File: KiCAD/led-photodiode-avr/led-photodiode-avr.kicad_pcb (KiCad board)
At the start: 4 copper layers, 68.6 x 80 mm, 85 parts, among them J1 Screw_Terminal_01x02, J2 Conn_02x08_Odd_Even, J3 ISP, J4 Conn_01x06_Pin, Q1 TTC1949, Q2 TTC1949, Q3 TTC1949, Q4 TTC1949, Q5 TTC1949, Q6 TTC1949, Q7 TTC1949, Q8 TTC1949, U1 REF3040AIDBZT, U10 AZ1117CH2-5.0, U11 MCP3221, U2 AZ1117CH2-5.0, U3 OPA365xxD, U5 DDC112, U6 LTC1380, U7 ATmega328-A, U8 OPA365AIDR, U9 LTC2631, Y1 CO_16MHZ

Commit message: working on v2 layout
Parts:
- removed N1: Optical_PCB, optical_pcb_model:optical_pcb
- added C27: 0.1uF, Capacitor_SMD:C_0805_2012Metric_Pad1.18x1.45mm_HandSolder, F.Cu at (150.5, 82.4)
- C19, C20, C24, C25: footprint Capacitor_SMD:C_0805_2012Metric_Pad1.18x1.45mm_HandSolder -> Capacitor_SMD:C_0603_1608Metric_Pad1.08x0.95mm_HandSolder
- moved TP4 77.0 mm to (126.5, 77.6)
- moved C24 67.0 mm to (158.5, 123.7), turned to 180 degrees
- moved TP1 65.0 mm to (137.7, 92.6)
- moved TP7 64.2 mm to (143.9, 106.8)
- moved TP3 62.2 mm to (139.8, 95.5)
- moved TP5 55.9 mm to (152.3, 97.8)
- moved TP6 54.4 mm to (152.3, 95.4)
- moved C25 53.8 mm to (162.9, 109.9)
- moved TP2 50.0 mm to (152.3, 93.1)
- moved C26 45.9 mm to (150.6, 75.8), turned to 180 degrees
- moved R12 45.8 mm to (156.6, 83.8), turned to -90 degrees
- moved U11 45.7 mm to (150.5, 79.1), turned to 180 degrees
- moved Q8 39.7 mm to (156.2, 89.5), turned to -90 degrees
- moved Q7 35.4 mm to (160.0, 89.5), turned to -90 degrees
- moved Q6 31.6 mm to (163.8, 89.5), turned to -90 degrees
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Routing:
- net /TSENSE: track 0.00 -> 34.6 mm, vias 0 -> 3
- net (no net): track 27.3 -> 0.00 mm
- net Net-(Q1-B): track 9.35 -> 30.2 mm, vias 0 -> 2
- net Net-(Q5-B): track 0.00 -> 20.7 mm, vias 0 -> 2
- net Net-(Q8-B): track 0.00 -> 19.5 mm, vias 0 -> 2
- net Net-(Q7-B): track 0.00 -> 18.9 mm, vias 0 -> 2
- net Net-(Q6-B): track 0.00 -> 18.3 mm, vias 0 -> 2
- net Net-(Q2-B): track 10.4 -> 27.6 mm, vias 0 -> 2
- net Net-(Q3-B): track 12.7 -> 26.1 mm, vias 0 -> 2
- net /LED_driver/LED_1: track 21.9 -> 8.78 mm, vias 1 -> 0
- net /PD7: track 38.5 -> 45.1 mm, vias 2 -> 3
- net /LED_driver/LED_2: track 1.27 -> 7.51 mm, vias 1 -> 0
- net /LED_driver/LED_8: track 0.00 -> 6.21 mm
- net Net-(Q4-B): track 16.7 -> 22.8 mm, vias 0 -> 2
- net /LED_driver/LED_5: track 0.00 -> 5.89 mm
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- added copper zone on F.Cu, net Net-(Q1-E)
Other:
- board text added: "NIR Wearable Optical Test V2.0 -2025-10 E. Hazen"
- board text removed: "NIR Wearable Optical Test V1.0 -2025-08 E. Hazen"

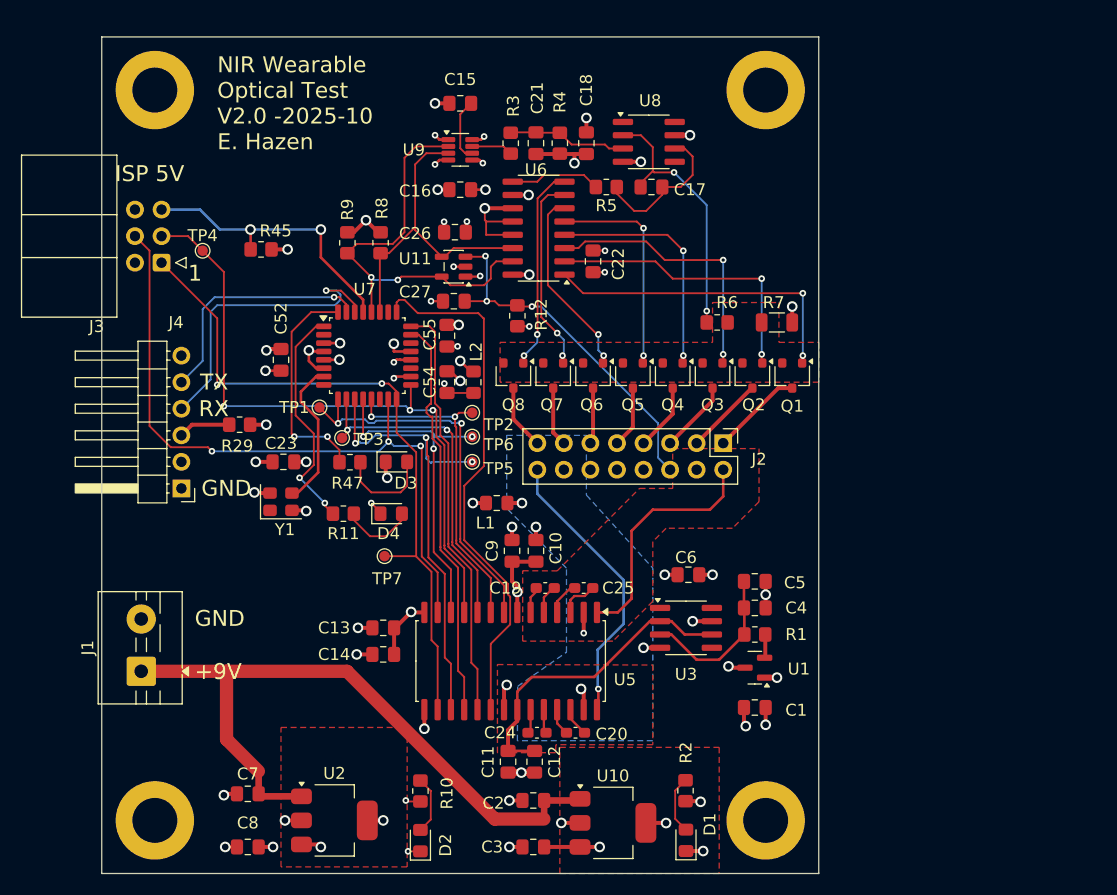
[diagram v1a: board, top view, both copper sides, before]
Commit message: Add op-amp buffer on temp sensor
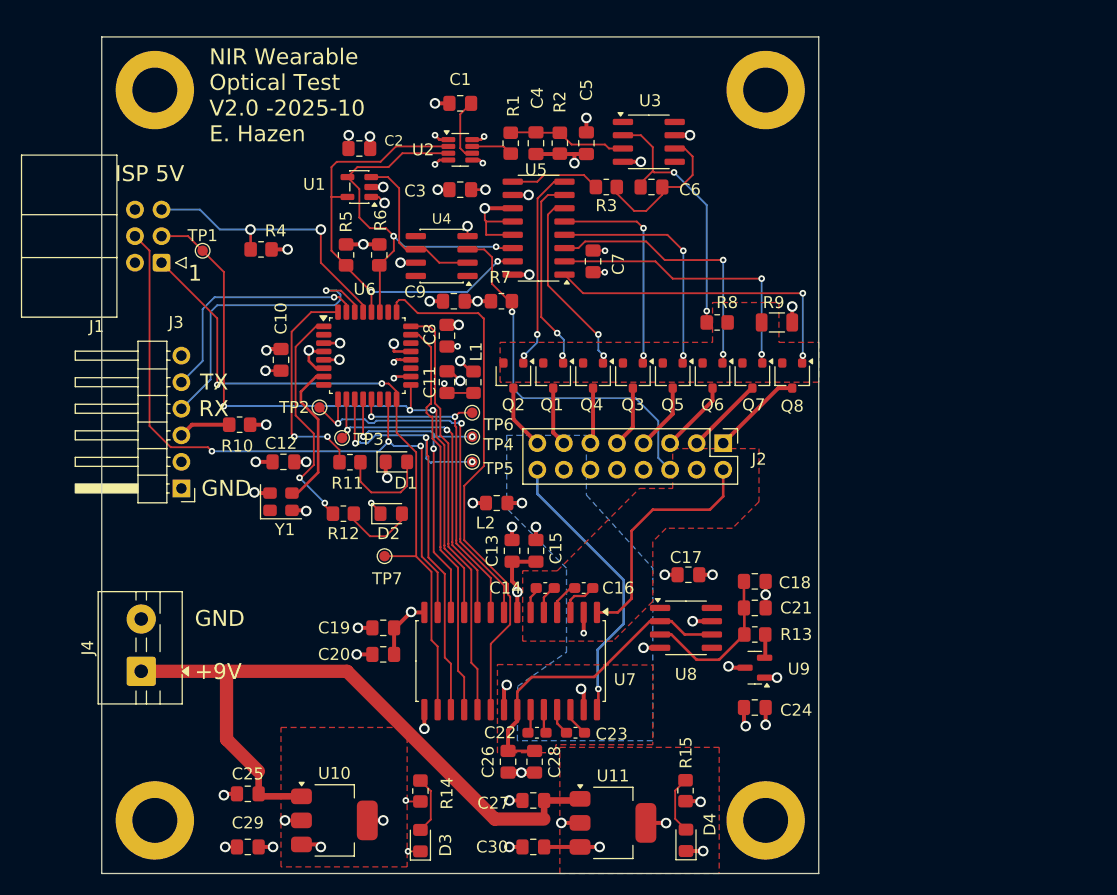
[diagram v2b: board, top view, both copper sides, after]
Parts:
- removed the C26 at (150.6, 75.8)
- added C2: 0.1uF, Capacitor_SMD:C_0805_2012Metric_Pad1.18x1.45mm_HandSolder, F.Cu at (141.5, 67.8)
- added U4: OPA365AIDR, Package_SO:SOIC-8_3.9x4.9mm_P1.27mm, F.Cu at (149.4, 78.1)
- U8: renamed from U3; value OPA365xxD -> OPA365AIDR
- moved U1 11.8 mm to (141.5, 71.5)
- moved R7 2.07 mm to (155.1, 82.4), turned to 0 degrees
- moved R5 1.17 mm to (140.2, 78.0)
- moved R6 1.17 mm to (143.4, 78.0)
- renumbered C15 to C1, C52 to C10, C54 to C11, C23 to C12, C9 to C13, C19 to C14, C10 to C15, C25 to C16, C6 to C17, C5 to C18, C13 to C19, C14 to C20, C4 to C21, C24 to C22, C20 to C23, C1 to C24, C7 to C25, C11 to C26, C2 to C27, C12 to C28, C8 to C29, C16 to C3, C3 to C30, C21 to C4, C18 to C5, C17 to C6, C22 to C7, C55 to C8, C27 to C9, D3 to D1, D4 to D2, D2 to D3, D1 to D4, J3 to J1, J4 to J3, J1 to J4, L2 to L1, L1 to L2, Q7 to Q1, Q8 to Q2, Q5 to Q3, Q6 to Q4, Q4 to Q5, Q3 to Q6, Q2 to Q7, Q1 to Q8, R3 to R1, R29 to R10, R47 to R11, R11 to R12, R1 to R13, R10 to R14, R2 to R15, R4 to R2, R5 to R3, R45 to R4, R9 to R5, R8 to R6, R12 to R7, R6 to R8, R7 to R9, TP4 to TP1, TP1 to TP2, TP6 to TP4, TP2 to TP6, U11 to U1, U2 to U10, U10 to U11, U9 to U2, U8 to U3, U6 to U5, U7 to U6, U5 to U7, U1 to U9
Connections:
- C9 pad 1: /TSENSE -> VCC
- J2 pad 6: /TSENSE -> Net-(J2-Pin_6)
- R7 pad 1: /TSENSE -> VCC
- R7 pad 2: Earth -> Net-(J2-Pin_6)
- U1 pad 3: /TSENSE -> Net-(U1-A_{IN})
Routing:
- net Net-(J2-Pin_6): track 0.00 -> 36.5 mm, vias 0 -> 1
- net /TSENSE: track 34.6 -> 0.00 mm, vias 3 -> 0
- net Net-(U1-A_{IN}): track 0.00 -> 15.7 mm
- net /SDA: track 30.6 -> 38.7 mm, vias 0 -> 2
- net /SCL: track 40.4 -> 43.7 mm
- net VCC: track 34.8 -> 38.1 mm, vias 17 -> 19
- net GND: track 47.2 -> 48.5 mm, vias 27 -> 28
- net Earth: track 43.8 -> 42.6 mm, vias 23 -> 22

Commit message: hopefully final Rev 2
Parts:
- moved C9 25.3 mm to (160.3, 59.1), turned to 0 degrees
- moved R7 22.1 mm to (169.2, 65.4), turned to 180 degrees
- moved U4 18.0 mm to (159.8, 63.4)
- moved U1 11.3 mm to (151.1, 65.7)
- moved C2 11.1 mm to (151.3, 62.5)
- moved C1 6.48 mm to (151.4, 70.0)
- moved C3 5.21 mm to (151.3, 77.0)
- moved U2 5.21 mm to (151.3, 73.2)
- moved C4 5.21 mm to (158.6, 72.5)
- moved C5 5.21 mm to (163.4, 72.5)
- moved C6 5.21 mm to (169.6, 76.7)
- moved R1 5.21 mm to (156.1, 72.5)
- moved R2 5.21 mm to (160.8, 72.5)
- moved R3 5.21 mm to (165.3, 76.7)
- moved U3 5.21 mm to (169.4, 72.4)
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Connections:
- C9 pad 1: VCC -> +5VA
- C9 pad 2: GND -> Earth
- R7 pad 1: VCC -> +5VA
- U4 pad 4: GND -> Earth
- U4 pad 7: VCC -> +5VA
- U5 pad 1: Net-(Q8-B) -> Net-(Q4-B)
- U5 pad 2: Net-(Q7-B) -> Net-(Q3-B)
- U5 pad 3: Net-(Q6-B) -> Net-(Q5-B)
- U5 pad 4: Net-(Q5-B) -> Net-(Q6-B)
- U5 pad 5: Net-(Q3-B) -> Net-(Q7-B)
- U5 pad 6: Net-(Q4-B) -> Net-(Q8-B)
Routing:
- net Net-(Q4-B): track 18.3 -> 5.36 mm, vias 2 -> 0
- net Net-(Q3-B): track 20.7 -> 9.63 mm, vias 2 -> 0
- net Net-(Q5-B): track 22.8 -> 14.2 mm, vias 2 -> 0
- net Net-(U3--): track 25.4 -> 18.9 mm
- net Net-(J2-Pin_6): track 36.5 -> 42.7 mm
- net Net-(Q1-B): track 18.9 -> 12.7 mm, vias 2 -> 0
- net Net-(Q2-B): track 19.5 -> 14.9 mm, vias 2 -> 0
- net VCC: track 38.1 -> 33.8 mm, vias 19 -> 17
- net Net-(U1-A_{IN}): track 15.7 -> 11.3 mm
- net /SDA: track 38.7 -> 42.9 mm, vias 2 -> 3
- net /SCL: track 43.7 -> 47.8 mm, vias 2 -> 3
- net Net-(Q6-B): track 26.1 -> 22.1 mm
- net +5VA: track 25.7 -> 29.7 mm, vias 11 -> 14
- net Earth: track 42.6 -> 45.2 mm, vias 22 -> 24
- net Net-(Q7-B): track 27.6 -> 25.2 mm
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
